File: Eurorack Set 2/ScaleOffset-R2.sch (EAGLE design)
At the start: 26 parts, among them IC3 TL074D

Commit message: More bodges... different led setup for scaleoffset, gaterhythm still has buttons reversed
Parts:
- added C2, C3: (no value), OPL:C-POLAR-A
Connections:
- removed net N$9: IC3D.OUT, LED1.C
- new net N$2: LED1.A, R7.2
- net -12V: now also C3.2
- net 12V: now also C2.1
- net GND: now also C2.2, C3.1, LED1.C; no longer R7.1
- net N$11: now also IC3D.OUT, R7.1; no longer LED1.A, R7.2
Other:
- moved on the sheet: LED1, R7
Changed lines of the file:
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@@
 <setting verticaltext="up"/>
 </settings>
-<grid distance="0.1" unitdist="inch" unit="inch" style="lines" multiple="1" display="no" altdistance="0.01" altunitdist="inch" altunit="inch"/>
+<grid distance="0.05" unitdist="inch" unit="inch" style="lines" multiple="1" display="no" altdistance="0.01" altunitdist="inch" altunit="inch"/>
 <layers>
 <layer number="1" name="Top" color="4" fill="1" visible="no" active="no"/>
@@
 <part name="R10" library="OPL" deviceset="R*" device="" value="51"/>
 <part name="R11" library="OPL" deviceset="R*" device="" value="51"/>
+<part name="C2" library="OPL" deviceset="C-POLAR*" device="-A"/>
+<part name="C3" library="OPL" deviceset="C-POLAR*" device="-A"/>
+<part name="GND18" library="SparkFun-Aesthetics" deviceset="GND" device=""/>
+<part name="GND19" library="SparkFun-Aesthetics" deviceset="GND" device=""/>
 </parts>
 <sheets>
@@
 <instance part="C1" gate="C" x="81.28" y="50.8"/>
 <instance part="GND8" gate="1" x="74.93" y="50.8" rot="R270"/>
-<instance part="LED1" gate="G$1" x="109.22" y="72.39" rot="R180"/>
-<instance part="R7" gate="R" x="88.9" y="68.58"/>
-<instance part="GND11" gate="1" x="80.01" y="62.23"/>
+<instance part="LED1" gate="G$1" x="128.27" y="78.74" rot="R90"/>
+<instance part="R7" gate="R" x="116.84" y="78.74"/>
+<instance part="GND11" gate="1" x="137.16" y="78.74" rot="R90"/>
 <instance part="OUT2" gate="G$1" x="166.37" y="93.98" rot="R180"/>
 <instance part="GND12" gate="1" x="149.86" y="91.44" rot="R270"/>
@@
 <instance part="R10" gate="R" x="143.51" y="121.92"/>
 <instance part="R11" gate="R" x="142.24" y="99.06"/>
+<instance part="C2" gate="C" x="99.06" y="26.67" rot="R270"/>
+<instance part="C3" gate="C" x="90.17" y="30.48" rot="R90"/>
+<instance part="GND18" gate="1" x="99.06" y="19.05"/>
+<instance part="GND19" gate="1" x="90.17" y="22.86"/>
 </instances>
 <busses>
@@
 </segment>
 <segment>
-<pinref part="R7" gate="R" pin="1"/>
-<wire x1="85.09" y1="68.58" x2="80.01" y2="68.58" width="0.1524" layer="91"/>
-<wire x1="80.01" y1="68.58" x2="80.01" y2="64.77" width="0.1524" layer="91"/>
-<pinref part="GND11" gate="1" pin="GND"/>
-</segment>
-<segment>
 <pinref part="OUT2" gate="G$1" pin="RING"/>
 <pinref part="GND12" gate="1" pin="GND"/>
@@
 <pinref part="GATE" gate="G$1" pin="RING"/>
 <pinref part="GND17" gate="1" pin="GND"/>
+</segment>
+<segment>
+<pinref part="LED1" gate="G$1" pin="C"/>
+<pinref part="GND11" gate="1" pin="GND"/>
+<wire x1="134.62" y1="78.74" x2="133.35" y2="78.74" width="0.1524" layer="91"/>
+</segment>
+<segment>
+<pinref part="C2" gate="C" pin="2"/>
+<pinref part="GND18" gate="1" pin="GND"/>
+</segment>
+<segment>
+<pinref part="C3" gate="C" pin="1"/>
+<pinref part="GND19" gate="1" pin="GND"/>
 </segment>
 </net>
@@
 <pinref part="IC3" gate="D" pin="+IN"/>
 <pinref part="IC3" gate="C" pin="-IN"/>
+<wire x1="93.98" y1="101.6" x2="93.98" y2="83.82" width="0.1524" layer="91"/>
+<wire x1="68.58" y1="101.6" x2="93.98" y2="101.6" width="0.1524" layer="91"/>
 </segment>
 </net>
@@
 <pinref part="U$5" gate="G$1" pin="+12V"/>
 <wire x1="85.09" y1="50.8" x2="85.09" y2="31.75" width="0.1524" layer="91"/>
-<wire x1="85.09" y1="31.75" x2="109.22" y2="31.75" width="0.1524" layer="91"/>
+<wire x1="85.09" y1="31.75" x2="99.06" y2="31.75" width="0.1524" layer="91"/>
+<wire x1="99.06" y1="31.75" x2="109.22" y2="31.75" width="0.1524" layer="91"/>
 <wire x1="109.22" y1="31.75" x2="109.22" y2="33.02" width="0.1524" layer="91"/>
 <label x="85.09" y="50.8" size="1.778" layer="95"/>
@@
 <pinref part="IC3" gate="P" pin="V+"/>
 <junction x="87.63" y="50.8"/>
+<pinref part="C2" gate="C" pin="1"/>
+<junction x="99.06" y="31.75"/>
 </segment>
 <segment>
@@
 <wire x1="100.33" y1="38.1" x2="92.71" y2="38.1" width="0.1524" layer="91"/>
 <wire x1="92.71" y1="38.1" x2="92.71" y2="35.56" width="0.1524" layer="91"/>
-<wire x1="92.71" y1="35.56" x2="87.63" y2="35.56" width="0.1524" layer="91"/>
+<wire x1="92.71" y1="35.56" x2="90.17" y2="35.56" width="0.1524" layer="91"/>
 <label x="96.52" y="36.83" size="1.778" layer="95"/>
 <pinref part="C4" gate="C" pin="1"/>
 <junction x="100.33" y="38.1"/>
 <pinref part="IC3" gate="P" pin="V-"/>
+<wire x1="90.17" y1="35.56" x2="87.63" y2="35.56" width="0.1524" layer="91"/>
 <wire x1="87.63" y1="35.56" x2="86.36" y2="35.56" width="0.1524" layer="91"/>
 <junction x="87.63" y="35.56"/>
+<pinref part="C3" gate="C" pin="2"/>
+<junction x="90.17" y="35.56"/>
 </segment>
 <segment>
@@
 </segment>
 </net>
-<net name="N$9" class="0">
-<segment>
-<pinref part="LED1" gate="G$1" pin="C"/>
-<wire x1="109.22" y1="77.47" x2="109.22" y2="81.28" width="0.1524" layer="91"/>
+<net name="N$11" class="0">
+<segment>
+<wire x1="93.98" y1="78.74" x2="93.98" y2="68.58" width="0.1524" layer="91"/>
+<pinref part="IC3" gate="D" pin="-IN"/>
 <pinref part="IC3" gate="D" pin="OUT"/>
-</segment>
-</net>
-<net name="N$11" class="0">
-<segment>
-<wire x1="93.98" y1="78.74" x2="93.98" y2="68.58" width="0.1524" layer="91"/>
-<pinref part="R7" gate="R" pin="2"/>
-<wire x1="92.71" y1="68.58" x2="93.98" y2="68.58" width="0.1524" layer="91"/>
-<pinref part="LED1" gate="G$1" pin="A"/>
-<wire x1="93.98" y1="68.58" x2="109.22" y2="68.58" width="0.1524" layer="91"/>
-<wire x1="109.22" y1="68.58" x2="109.22" y2="69.85" width="0.1524" layer="91"/>
-<junction x="93.98" y="68.58"/>
-<pinref part="IC3" gate="D" pin="-IN"/>
+<wire x1="109.22" y1="81.28" x2="113.03" y2="81.28" width="0.1524" layer="91"/>
+<pinref part="R7" gate="R" pin="1"/>
+<wire x1="113.03" y1="81.28" x2="113.03" y2="78.74" width="0.1524" layer="91"/>
+<wire x1="113.03" y1="78.74" x2="113.03" y2="68.58" width="0.1524" layer="91"/>
+<wire x1="113.03" y1="68.58" x2="93.98" y2="68.58" width="0.1524" layer="91"/>
+<junction x="113.03" y="78.74"/>
 </segment>
 </net>
@@
 </segment>
 </net>
+<net name="N$2" class="0">
+<segment>
+<pinref part="LED1" gate="G$1" pin="A"/>
+<wire x1="120.65" y1="78.74" x2="125.73" y2="78.74" width="0.1524" layer="91"/>
+<pinref part="R7" gate="R" pin="2"/>
+</segment>
+</net>

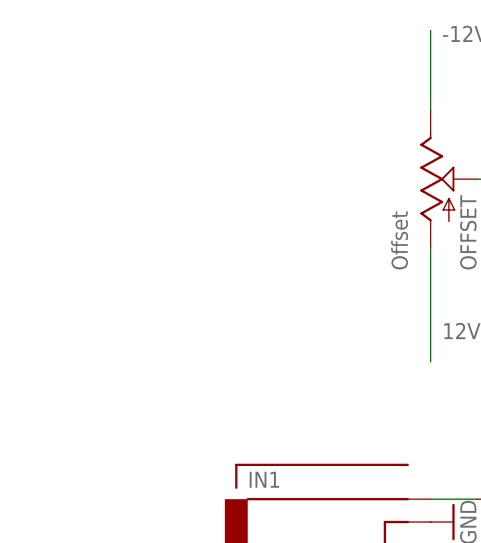
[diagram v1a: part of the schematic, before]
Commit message: Fiducials!
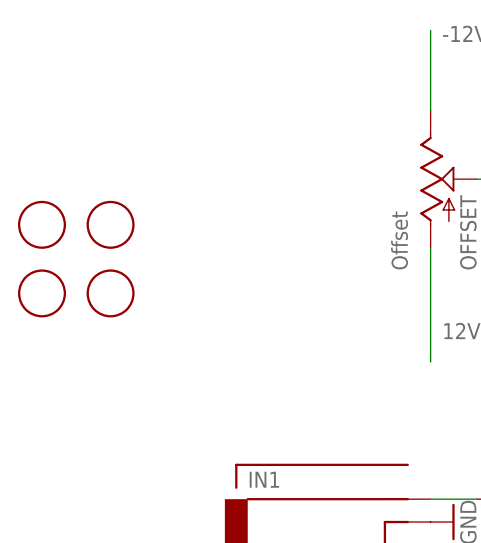
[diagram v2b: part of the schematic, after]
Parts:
- added U$1, U$2, U$3, U$4: FIDUCIAL, adafruit:FIDUCIAL
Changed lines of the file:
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@@
 <setting verticaltext="up"/>
 </settings>
-<grid distance="0.05" unitdist="inch" unit="inch" style="lines" multiple="1" display="no" altdistance="0.01" altunitdist="inch" altunit="inch"/>
+<grid distance="0.1" unitdist="inch" unit="inch" style="lines" multiple="1" display="no" altdistance="0.01" altunitdist="inch" altunit="inch"/>
 <layers>
 <layer number="1" name="Top" color="4" fill="1" visible="no" active="no"/>
@@
 <part name="GND18" library="SparkFun-Aesthetics" deviceset="GND" device=""/>
 <part name="GND19" library="SparkFun-Aesthetics" deviceset="GND" device=""/>
+<part name="U$1" library="adafruit" deviceset="FIDUCIAL" device=""/>
+<part name="U$2" library="adafruit" deviceset="FIDUCIAL" device=""/>
+<part name="U$3" library="adafruit" deviceset="FIDUCIAL" device=""/>
+<part name="U$4" library="adafruit" deviceset="FIDUCIAL" device=""/>
 </parts>
 <sheets>
@@
 <instance part="GND18" gate="1" x="99.06" y="19.05"/>
 <instance part="GND19" gate="1" x="90.17" y="22.86"/>
+<instance part="U$1" gate="G$1" x="-5.08" y="147.32"/>
+<instance part="U$2" gate="G$1" x="2.54" y="147.32"/>
+<instance part="U$3" gate="G$1" x="-5.08" y="139.7"/>
+<instance part="U$4" gate="G$1" x="2.54" y="139.7"/>
 </instances>
 <busses>
